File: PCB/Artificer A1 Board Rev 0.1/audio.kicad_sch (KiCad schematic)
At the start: 1 part, among them CN1 PJ-3220-B

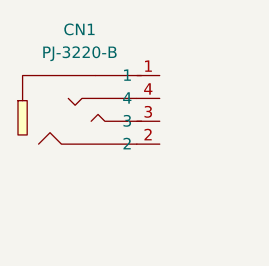
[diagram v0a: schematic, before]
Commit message: localized libraries
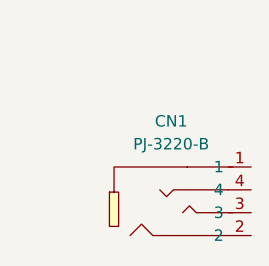
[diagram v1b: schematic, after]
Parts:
- removed CN1: PJ-3220-B, easyeda2kicad:AUDIO-TH_PJ-3220-Y, symbol easyeda2kicad:PJ-3220-B
- added CN1: PJ-3220-B, easyeda:AUDIO-TH_PJ-3220-Y, symbol easyeda:PJ-3220-B
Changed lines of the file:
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@@
 	)
 	(symbol
-		(lib_id "easyeda2kicad:PJ-3220-B")
-		(at 129.54 91.44 0)
+		(lib_id "easyeda:PJ-3220-B")
+		(at 139.7 101.6 0)
 		(unit 1)
 		(exclude_from_sim no)
@@
 		(fields_autoplaced yes)
 		(property "Reference" "CN1"
-			(at 128.27 82.55 0)
+			(at 138.43 92.71 0)
 			(effects
 				(font
@@
 		)
 		(property "Value" "PJ-3220-B"
-			(at 128.27 85.09 0)
+			(at 138.43 95.25 0)
 			(effects
 				(font
@@
 			)
 		)
-		(property "Footprint" "easyeda2kicad:AUDIO-TH_PJ-3220-Y"
-			(at 129.54 102.87 0)
+		(property "Footprint" "easyeda:AUDIO-TH_PJ-3220-Y"
+			(at 139.7 113.03 0)
 			(effects
 				(font
@@
 		)
 		(property "Datasheet" ""
-			(at 129.54 91.44 0)
+			(at 139.7 101.6 0)
 			(effects
 				(font
@@
 		)
 		(property "Description" ""
-			(at 129.54 91.44 0)
+			(at 139.7 101.6 0)
 			(effects
 				(font
@@
 		)
 		(property "LCSC Part" "C2885035"
-			(at 129.54 105.41 0)
+			(at 139.7 115.57 0)
 			(effects
 				(font
@@
 		(pin "1"
 		)
-		(pin "2"
-		)
 		(pin "4"
 		)
 		(pin "3"
 		)
+		(pin "2"
+		)
 		(instances

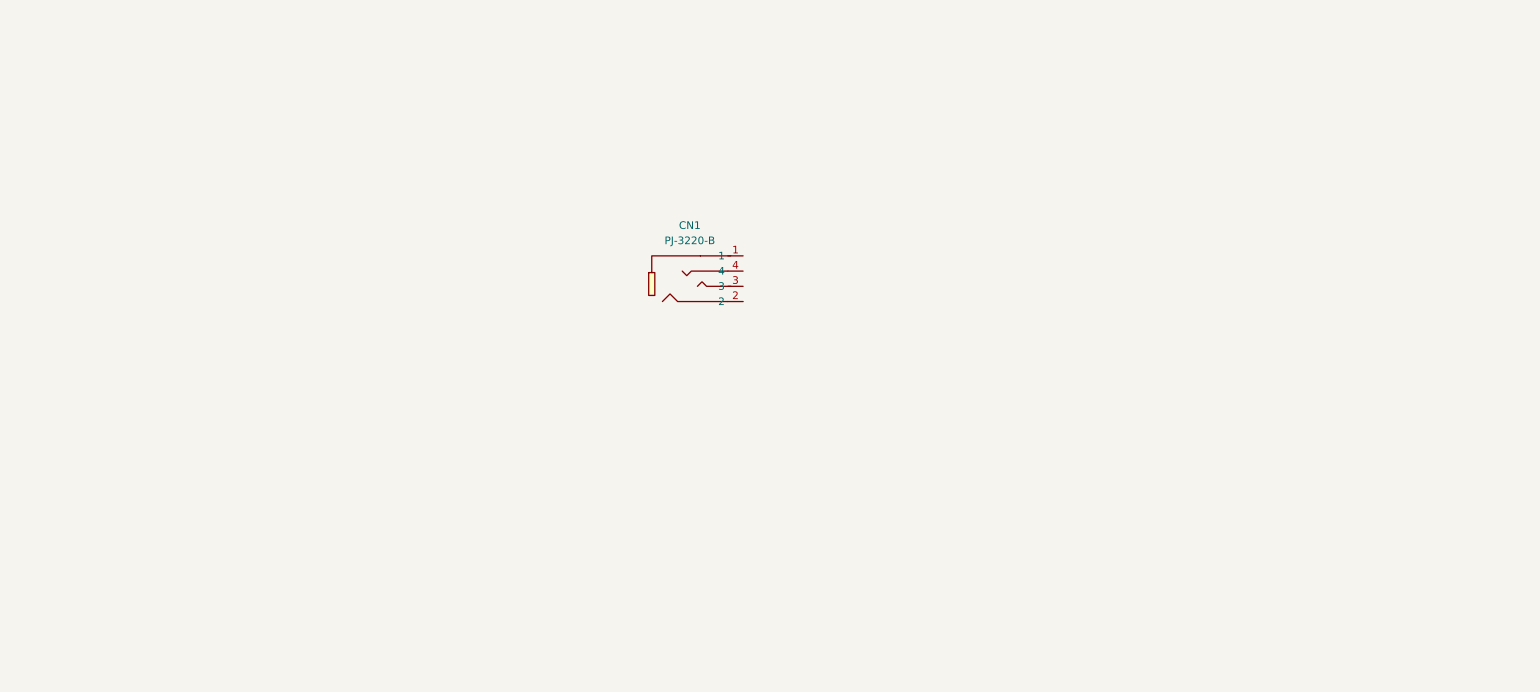
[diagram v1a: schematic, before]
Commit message: added HDMI, DP, DSI, etc
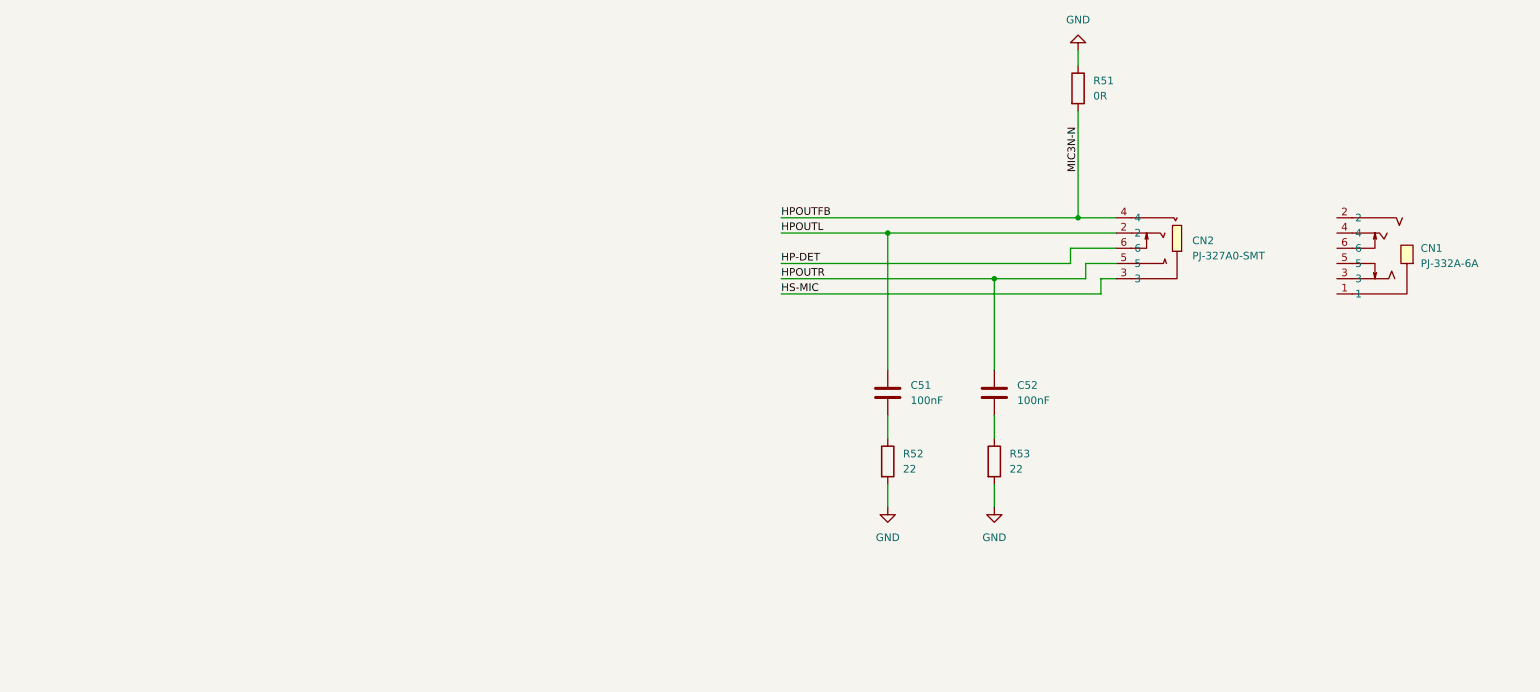
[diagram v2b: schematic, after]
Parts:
- removed CN1: PJ-3220-B, easyeda:AUDIO-TH_PJ-3220-Y, symbol easyeda:PJ-3220-B
- added C51, C52: 100nF, symbol Device:C
- added CN1: PJ-332A-6A, easyeda:AUDIO-SMD_PJ-332A-6A, symbol easyeda:PJ-332A-6A
- added CN2: PJ-327A0-SMT, easyeda:AUDIO-SMD_PJ-327A0-SMT, symbol easyeda:PJ-327A0-SMT
- added R51: 0R, symbol Device:R
- added R52, R53: 22, symbol Device:R
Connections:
- new net: C52.2, R53.1
- new net: C51.2, R52.1
- new net GND: R51.1, R52.2, R53.2
- new net HP-DET: CN2.6
- new net HPOUTFB: CN2.4, R51.2
- new net HPOUTL: C51.1, CN2.2
- new net HPOUTR: C52.1, CN2.5
- new net HS-MIC: CN2.3

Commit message: added: sd, wifi, audio, started power, fixed buses
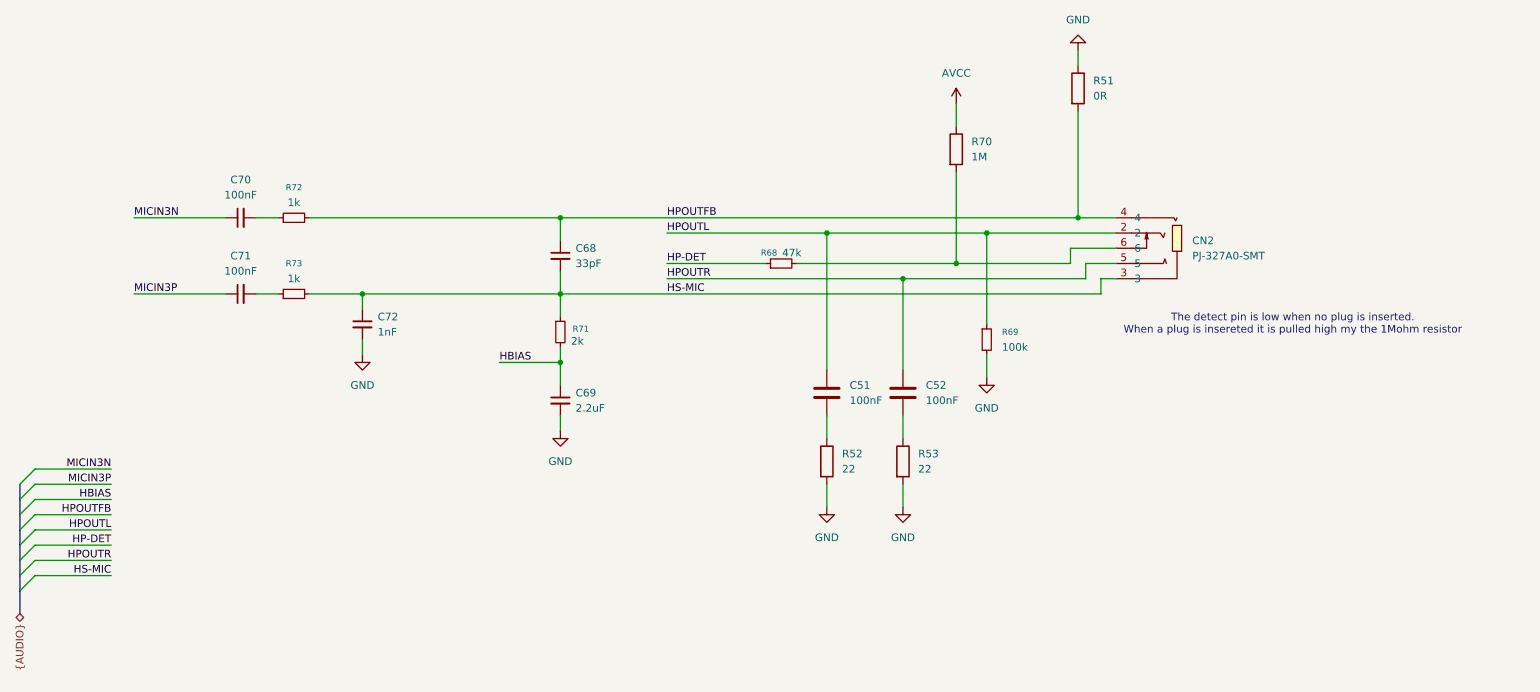
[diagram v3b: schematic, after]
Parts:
- removed CN1: PJ-332A-6A, easyeda:AUDIO-SMD_PJ-332A-6A, symbol easyeda:PJ-332A-6A
- added C68: 33pF, symbol Device:C_Small
- added C69: 2.2uF, symbol Device:C_Small
- added C70, C71: 100nF, symbol Device:C_Small
- added C72: 1nF, symbol Device:C_Small
- added R68: 47k, symbol Device:R_Small
- added R69: 100k, symbol Device:R_Small
- added R70: 1M, symbol Device:R
- added R71: 2k, symbol Device:R_Small
- added R72, R73: 1k, symbol Device:R_Small
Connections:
- net GND: now also C69.2, C72.2, R69.2
- net HP-DET: now also R68.1; no longer CN2.6
- net HPOUTFB: now also C68.1, R72.2
- net HPOUTL: now also R69.1
- net HS-MIC: now also C68.2, C72.1, R71.1, R73.2
- new net: CN2.6, R68.2, R70.2
- new net: C71.2, R73.1
- new net: C70.2, R72.1
- new net AVCC: R70.1
- new net HBIAS: C69.1, R71.2
- new net MICIN3N: C70.1
- new net MICIN3P: C71.1
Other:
- note added: "The detect pin is low when no plug is inserted. When a plug is insereted it is pulled high my the 1Mohm resistor"
- moved on the sheet: C51, C52, R52, R53
